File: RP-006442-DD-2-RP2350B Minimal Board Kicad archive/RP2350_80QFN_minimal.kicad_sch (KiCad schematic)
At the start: 51 parts, among them J1 USB_C_Receptacle_USB2.0_16P, J2 Conn_02x26_Odd_Even, J3 Conn_02x26_Odd_Even, J4 SM03B-SRSS-TB, SW1 SW_Push, SW2 SW_Push, U1 RP2350_80QFN, U2 NCP1117-3.3_SOT223, U3 W25Q128JVS, U4 DNF, Y1 ABM8-272-T3

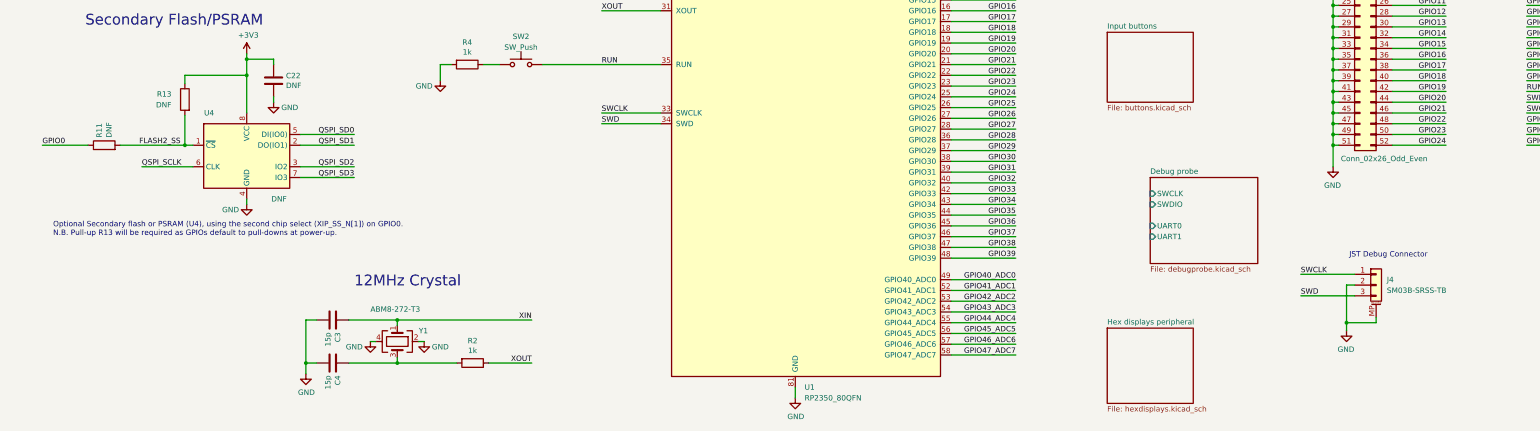
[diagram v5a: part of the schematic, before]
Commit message: Added debugger labels to root
moved some symbols around
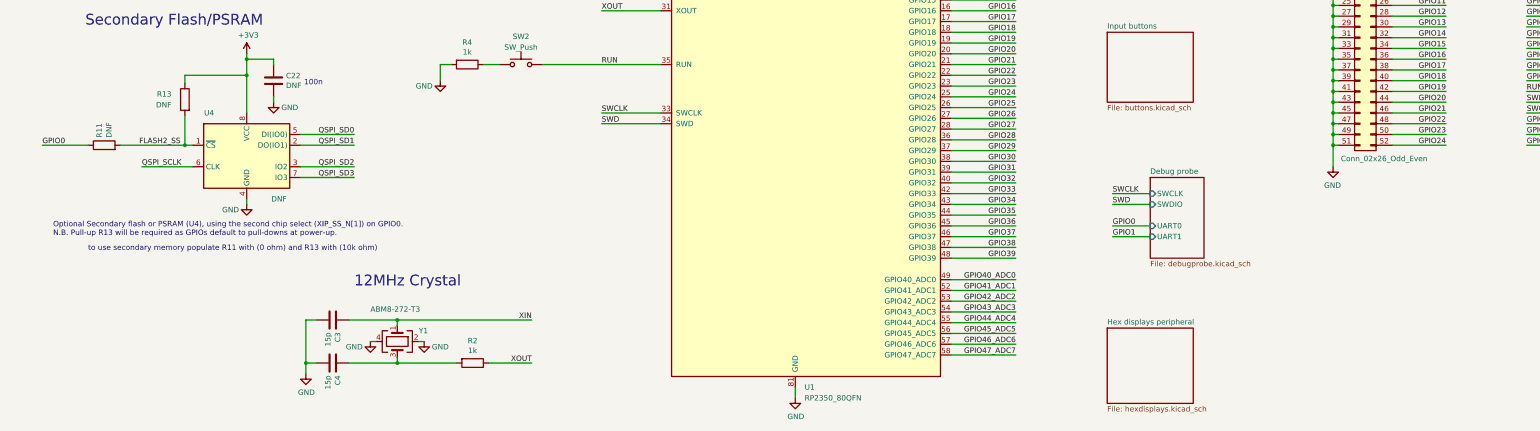
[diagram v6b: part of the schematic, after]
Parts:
- removed J4: SM03B-SRSS-TB, Connector_JST:JST_SH_SM03B-SRSS-TB_1x03-1MP_P1.00mm_Horizontal, symbol Connector_Generic_MountingPin:Conn_01x03_MountingPin
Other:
- note added: "100n"
- note added: "to use secondary memory populate R11 with (0 ohm) and R13 with (10k ohm)"
- note removed: "JST Debug Connector"
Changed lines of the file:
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@@
 		)
 	)
-	(text "JST Debug Connector"
+	(text "100n"
 		(exclude_from_sim no)
-		(at 328.93 210.82 0)
+		(at 84.328 169.418 0)
 		(effects
 			(font
 				(size 1.27 1.27)
 			)
-			(justify left bottom)
 		)
 	)
@@
 		)
 	)
+	(text "to use secondary memory populate R11 with (0 ohm) and R13 with (10k ohm)"
+		(exclude_from_sim no)
+		(at 65.278 208.534 0)
+		(effects
+			(font
+				(size 1.27 1.27)
+			)
+		)
+	)
 	(junction
 		(at 119.38 115.57)
@@
 	)
 	(junction
-		(at 328.295 226.06)
-		(diameter 0)
-		(color 0 0 0 0)
-	)
-	(junction
 		(at 325.12 130.81)
 		(diameter 0)
@@
 	(wire
 		(pts
-			(xy 330.2 217.17) (xy 328.295 217.17)
-		)
-		(stroke
-			(width 0)
-			(type default)
-		)
-	)
-	(wire
-		(pts
 			(xy 46.99 59.69) (xy 58.42 59.69)
 		)
@@
 	(wire
 		(pts
-			(xy 328.295 226.06) (xy 328.295 227.965)
-		)
-		(stroke
-			(width 0)
-			(type default)
-		)
-	)
-	(wire
-		(pts
 			(xy 397.51 166.37) (xy 397.51 168.91)
 		)
@@
 	(wire
 		(pts
+			(xy 273.05 198.12) (xy 281.94 198.12)
+		)
+		(stroke
+			(width 0)
+			(type default)
+		)
+	)
+	(wire
+		(pts
 			(xy 80.01 132.715) (xy 92.71 132.715)
 		)
@@
 	(wire
 		(pts
-			(xy 335.28 224.79) (xy 335.28 226.06)
+			(xy 273.05 203.2) (xy 281.94 203.2)
 		)
 		(stroke
@@
 	(wire
 		(pts
-			(xy 328.295 217.17) (xy 328.295 226.06)
-		)
-		(stroke
-			(width 0)
-			(type default)
-		)
-	)
-	(wire
-		(pts
 			(xy 397.51 133.35) (xy 397.51 135.89)
 		)
@@
 	(wire
 		(pts
-			(xy 317.5 214.63) (xy 330.2 214.63)
-		)
-		(stroke
-			(width 0)
-			(type default)
-		)
-	)
-	(wire
-		(pts
 			(xy 68.58 162.56) (xy 68.58 163.83)
 		)
@@
 	(wire
 		(pts
-			(xy 328.295 226.06) (xy 335.28 226.06)
-		)
-		(stroke
-			(width 0)
-			(type default)
-		)
-	)
-	(wire
-		(pts
 			(xy 326.39 123.19) (xy 325.12 123.19)
 		)
@@
 	(wire
 		(pts
+			(xy 273.05 195.58) (xy 281.94 195.58)
+		)
+		(stroke
+			(width 0)
+			(type default)
+		)
+	)
+	(wire
+		(pts
 			(xy 351.79 125.73) (xy 339.09 125.73)
 		)
@@
 	(wire
 		(pts
-			(xy 317.5 219.71) (xy 330.2 219.71)
-		)
-		(stroke
-			(width 0)
-			(type default)
-		)
-	)
-	(wire
-		(pts
 			(xy 21.59 78.74) (xy 21.59 80.01)
 		)
@@
 	(wire
 		(pts
+			(xy 273.05 205.74) (xy 281.94 205.74)
+		)
+		(stroke
+			(width 0)
+			(type default)
+		)
+	)
+	(wire
+		(pts
 			(xy 303.53 129.54) (xy 303.53 130.81)
 		)
@@
 		)
 	)
+	(label "GPIO0"
+		(at 273.05 203.2 0)
+		(effects
+			(font
+				(size 1.27 1.27)
+			)
+			(justify left bottom)
+		)
+	)
 	(label "GPIO13"
 		(at 250.19 144.78 180)
@@
 		)
 	)
-	(label "SWD"
-		(at 317.5 219.71 0)
-		(effects
-			(font
-				(size 1.27 1.27)
-			)
-			(justify left bottom)
-		)
-	)
 	(label "QSPI_SD0"
 		(at 152.4 127 0)
@@
 		)
 	)
+	(label "GPIO1"
+		(at 273.05 205.74 0)
+		(effects
+			(font
+				(size 1.27 1.27)
+			)
+			(justify left bottom)
+		)
+	)
 	(label "USB_D-"
 		(at 267.97 104.14 180)
@@
 		)
 	)
+	(label "SWCLK"
+		(at 273.05 195.58 0)
+		(effects
+			(font
+				(size 1.27 1.27)
+			)
+			(justify left bottom)
+		)
+	)
 	(label "GPIO28"
 		(at 250.19 182.88 180)
@@
 		)
 	)
+	(label "SWD"
+		(at 273.05 198.12 0)
+		(effects
+			(font
+				(size 1.27 1.27)
+			)
+			(justify left bottom)
+		)
+	)
 	(label "QSPI_SD1"
 		(at 93.98 184.15 180)
@@
 		)
 	)
-	(label "SWCLK"
-		(at 317.5 214.63 0)
-		(effects
-			(font
-				(size 1.27 1.27)
-			)
-			(justify left bottom)
-		)
-	)
 	(label "GPIO4"
 		(at 351.79 133.35 180)
@@
 	(symbol
 		(lib_id "power:GND")
-		(at 328.295 227.965 0)
-		(mirror y)
-		(unit 1)
-		(exclude_from_sim no)
-		(in_bom yes)
-		(on_board yes)
-		(dnp no)
-		(property "Reference" "#PWR032"
-			(at 328.295 234.315 0)
-			(effects
-				(font
-					(size 1.27 1.27)
-				)
-				(hide yes)
-			)
-		)
-		(property "Value" "GND"
-			(at 328.168 232.3592 0)
-			(effects
-				(font
-					(size 1.27 1.27)
-				)
-			)
-		)
-		(property "Footprint" ""
-			(at 328.295 227.965 0)
-			(effects
-				(font
-					(size 1.27 1.27)
-				)
-				(hide yes)
-			)
-		)
-		(property "Datasheet" ""
-			(at 328.295 227.965 0)
-			(effects
-				(font
-					(size 1.27 1.27)
-				)
-				(hide yes)
-			)
-		)
-		(property "Description" ""
-			(at 328.295 227.965 0)
-			(effects
-				(font
-					(size 1.27 1.27)
-				)
-				(hide yes)
-			)
-		)
-		(pin "1"
-		)
-		(instances
-			(project "RP2350_80QFN_minimal"
-				(path "/94683f5c-9cd9-448e-be96-9792537b5cb8"
-					(reference "#PWR032")
-					(unit 1)
-				)
-			)
-		)
-	)
-	(symbol
-		(lib_id "power:GND")
 		(at 74.93 173.99 0)
 		(unit 1)
@@
 	)
 	(symbol
-		(lib_id "Connector_Generic_MountingPin:Conn_01x03_MountingPin")
-		(at 335.28 217.17 0)
-		(unit 1)
-		(exclude_from_sim no)
-		(in_bom yes)
-		(on_board yes)
-		(dnp no)
-		(fields_autoplaced yes)
-		(property "Reference" "J4"
-			(at 337.82 215.9 0)
-			(effects
-				(font
-					(size 1.27 1.27)
-				)
-				(justify left)
-			)
-		)
-		(property "Value" "SM03B-SRSS-TB"
-			(at 337.82 218.44 0)
-			(effects
-				(font
-					(size 1.27 1.27)
-				)
-				(justify left)
-			)
-		)
-		(property "Footprint" "Connector_JST:JST_SH_SM03B-SRSS-TB_1x03-1MP_P1.00mm_Horizontal"
-			(at 335.28 217.17 0)
-			(effects
-				(font
-					(size 1.27 1.27)
-				)
-				(hide yes)
-			)
-		)
-		(property "Datasheet" "~"
-			(at 335.28 217.17 0)
-			(effects
-				(font
-					(size 1.27 1.27)
-				)
-				(hide yes)
-			)
-		)
-		(property "Description" ""
-			(at 335.28 217.17 0)
-			(effects
-				(font
-					(size 1.27 1.27)
-				)
-				(hide yes)
-			)
-		)
-		(pin "1"
-		)
-		(pin "2"
-		)
-		(pin "3"
-		)
-		(pin "MP"
-		)
-		(instances
-			(project "RP2350_80QFN_minimal"
-				(path "/94683f5c-9cd9-448e-be96-9792537b5cb8"
-					(reference "J4")
-					(unit 1)
-				)
-			)
-		)
-	)
-	(symbol
 		(lib_id "Device:C")
 		(at 154.94 66.04 0)
@@
 	(sheet
 		(at 281.94 191.77)
-		(size 25.4 20.32)
+		(size 12.7 19.05)
 		(exclude_from_sim no)
 		(in_bom yes)
@@
 		)
 		(property "Sheetfile" "debugprobe.kicad_sch"
-			(at 281.94 212.6746 0)
+			(at 281.94 211.4046 0)
 			(effects
 				(font

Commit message: Added debugprobe components to pcb
added pinheader connector to debug probe
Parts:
- R12, R5: footprint (none) -> Resistor_SMD:R_0402_1005Metric
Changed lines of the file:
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@@
 			)
 		)
-		(property "Footprint" ""
+		(property "Footprint" "Resistor_SMD:R_0402_1005Metric"
 			(at 48.26 42.672 90)
 			(effects
@@
 			)
 		)
-		(property "Footprint" ""
+		(property "Footprint" "Resistor_SMD:R_0402_1005Metric"
 			(at 57.15 45.212 90)
 			(effects

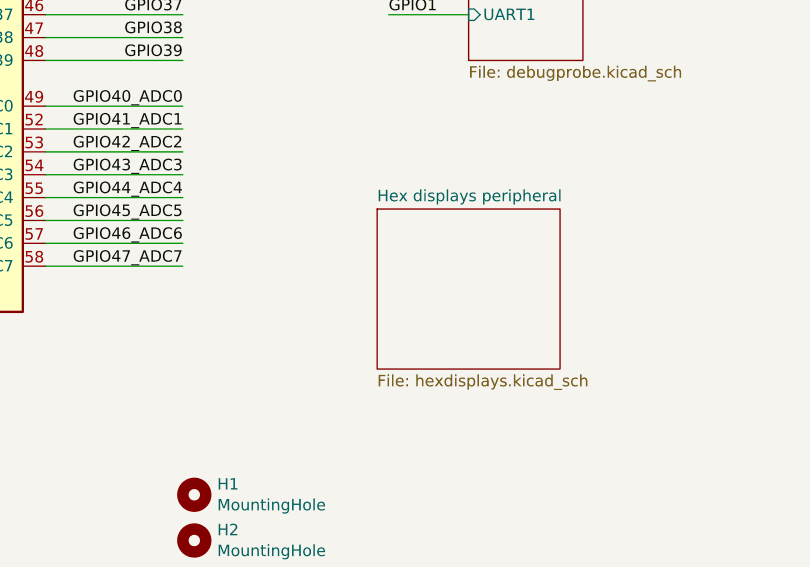
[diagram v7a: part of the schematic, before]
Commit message: Update hex displays
Added 7-segment display symbol, labels, i2c pull-up resistors, capacitor.

Synced added components to pcb.
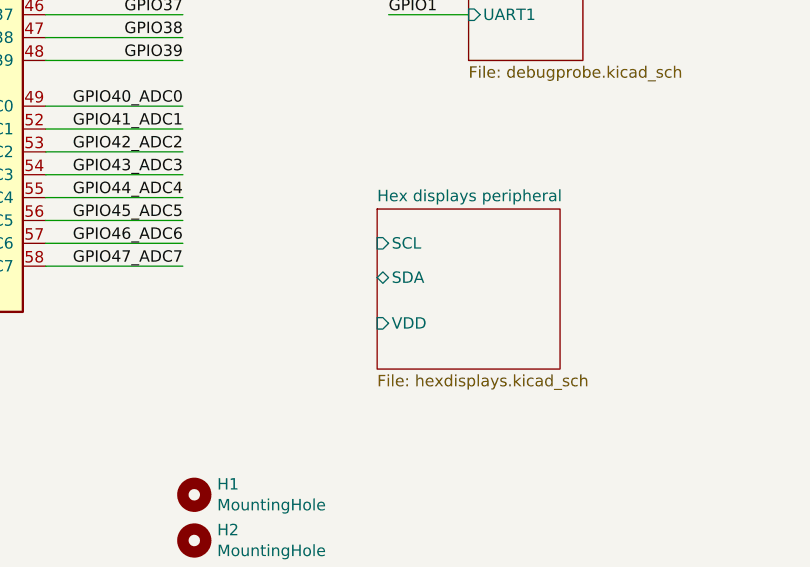
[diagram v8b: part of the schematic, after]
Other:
- sheet Hex displays peripheral ports: added SCL, SDA, VDD; removed none
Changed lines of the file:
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@@
+			)
+		)
+		(pin "SCL" input
+			(at 271.78 231.14 180)
+			(effects
+				(font
+					(size 1.27 1.27)
+				)
+				(justify left)
+			)
+		)
+		(pin "SDA" bidirectional
+			(at 271.78 234.95 180)
+			(effects
+				(font
+					(size 1.27 1.27)
+				)
+				(justify left)
+			)
+		)
+		(pin "VDD" input
+			(at 271.78 240.03 180)
+			(effects
+				(font
+					(size 1.27 1.27)
+				)
+				(justify left)
 			)
 		)
